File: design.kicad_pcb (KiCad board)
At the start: 2 copper layers, 136.2 x 88.1 mm, 170 parts, among them J1 TYPE-C-31-M-12, U1 TTP223, U10 ATtiny1616-M, U2 TTP223, U3 TTP223, U4 TTP223, U5 TTP223, U6 TTP223, U7 TTP223, U8 TTP223, U9 MAX77751CEFG_T

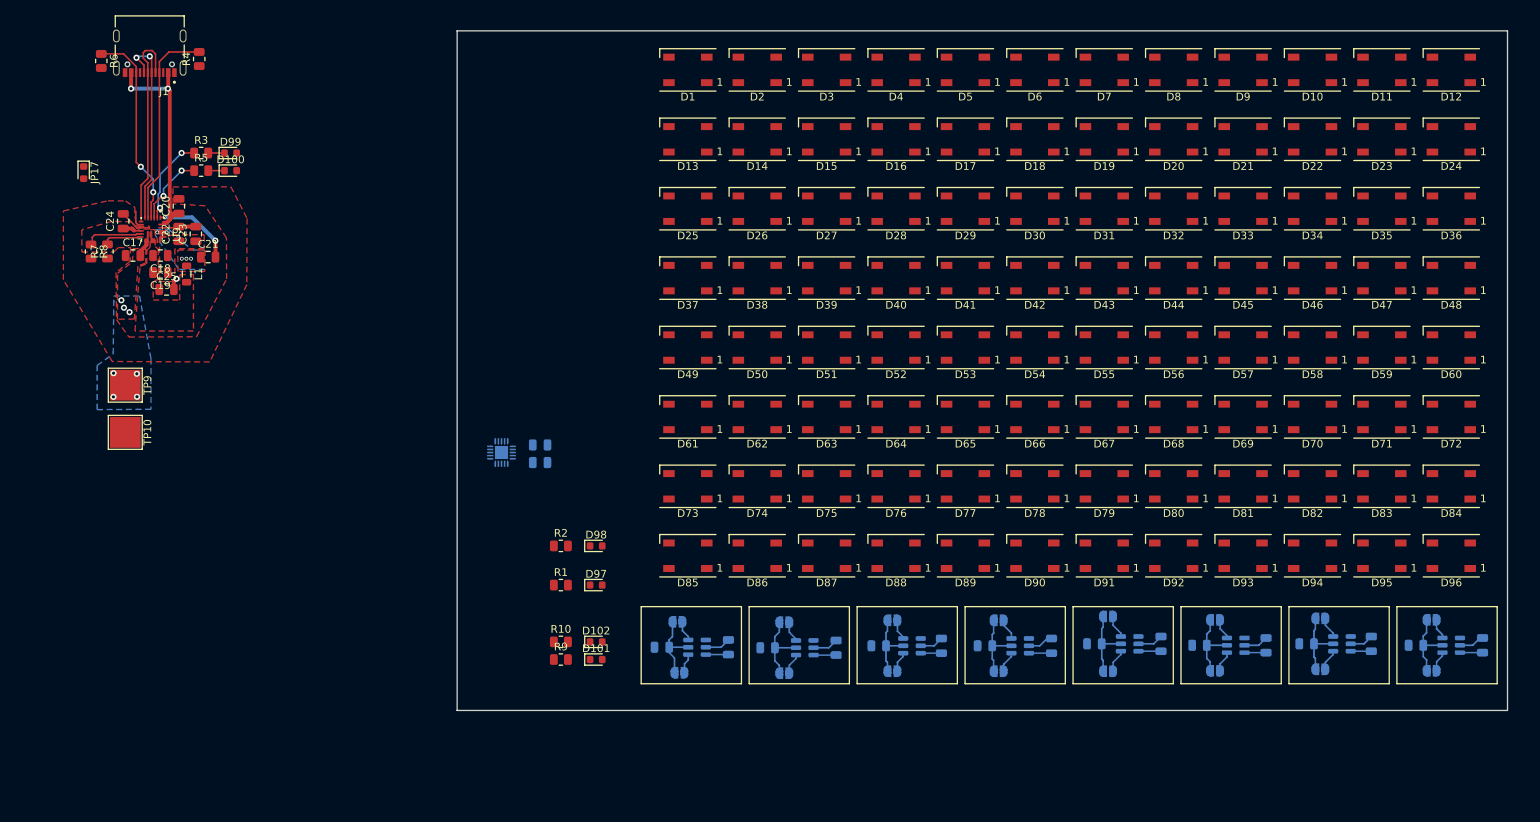
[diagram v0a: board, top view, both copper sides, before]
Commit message: some confusing LED double footprints
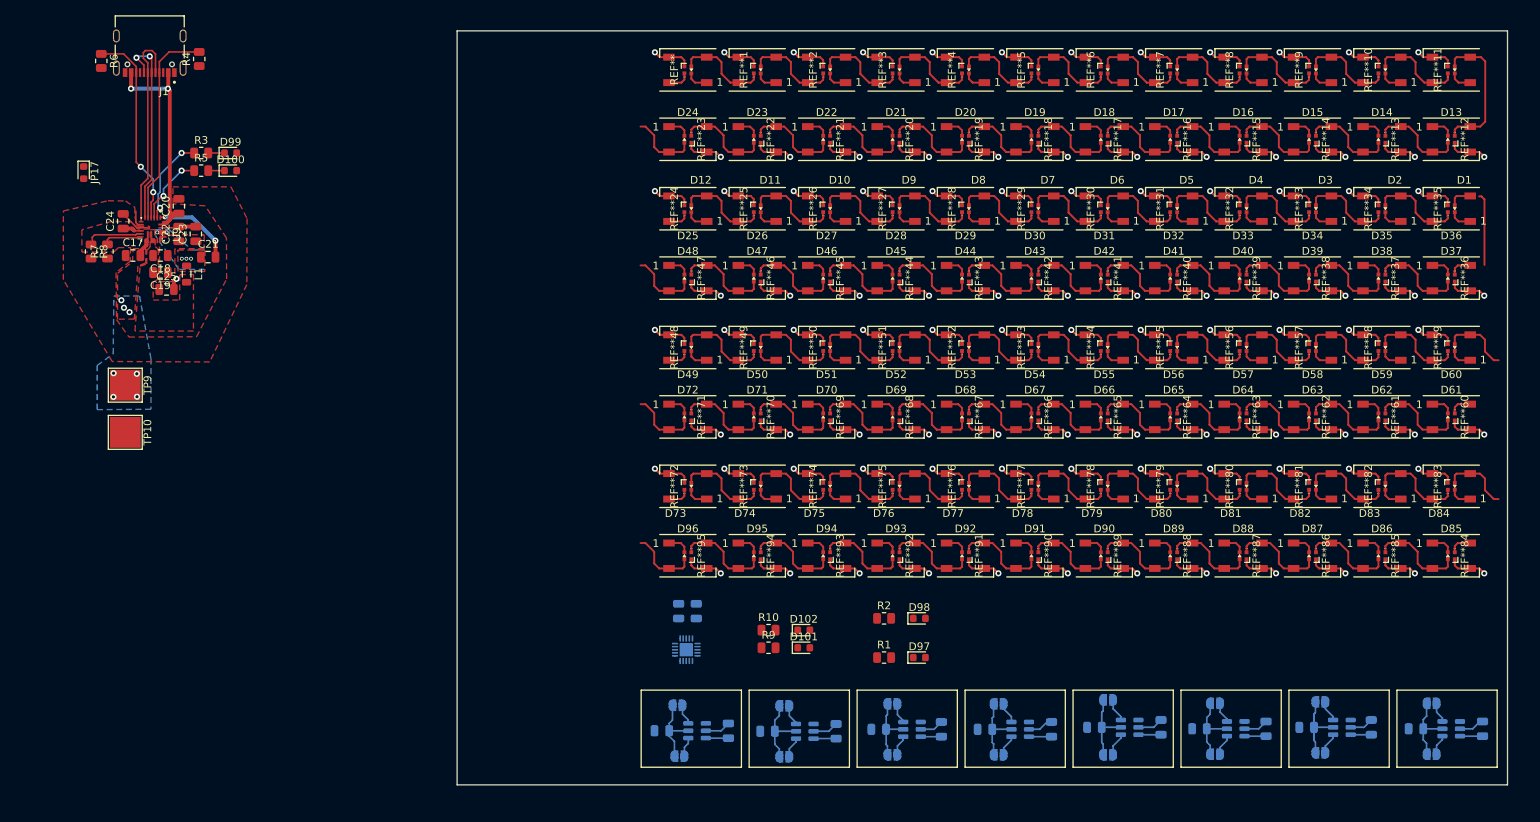
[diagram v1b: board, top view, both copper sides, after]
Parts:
- added REF**: LED_SK6805_EC15_1.5x1.5mm, LED_custom:LED_SK6805_EC15_1.5x1.5mm, F.Cu at (139.4, 57.4)
- added REF**1: LED_SK6805_EC15_1.5x1.5mm, LED_custom:LED_SK6805_EC15_1.5x1.5mm, F.Cu at (148.4, 57.4)
- added REF**10: LED_SK6805_EC15_1.5x1.5mm, LED_custom:LED_SK6805_EC15_1.5x1.5mm, F.Cu at (229.4, 57.4)
- added REF**11: LED_SK6805_EC15_1.5x1.5mm, LED_custom:LED_SK6805_EC15_1.5x1.5mm, F.Cu at (238.4, 57.4)
- added REF**12: LED_SK6805_EC15_1.5x1.5mm, LED_custom:LED_SK6805_EC15_1.5x1.5mm, F.Cu at (238.4, 66.4)
- added REF**13: LED_SK6805_EC15_1.5x1.5mm, LED_custom:LED_SK6805_EC15_1.5x1.5mm, F.Cu at (229.4, 66.4)
- added REF**14: LED_SK6805_EC15_1.5x1.5mm, LED_custom:LED_SK6805_EC15_1.5x1.5mm, F.Cu at (220.4, 66.4)
- added REF**15: LED_SK6805_EC15_1.5x1.5mm, LED_custom:LED_SK6805_EC15_1.5x1.5mm, F.Cu at (211.4, 66.4)
- added REF**16: LED_SK6805_EC15_1.5x1.5mm, LED_custom:LED_SK6805_EC15_1.5x1.5mm, F.Cu at (202.4, 66.4)
- added REF**17: LED_SK6805_EC15_1.5x1.5mm, LED_custom:LED_SK6805_EC15_1.5x1.5mm, F.Cu at (193.4, 66.4)
- added REF**18: LED_SK6805_EC15_1.5x1.5mm, LED_custom:LED_SK6805_EC15_1.5x1.5mm, F.Cu at (184.4, 66.4)
- added REF**19: LED_SK6805_EC15_1.5x1.5mm, LED_custom:LED_SK6805_EC15_1.5x1.5mm, F.Cu at (175.4, 66.4)
- added REF**2: LED_SK6805_EC15_1.5x1.5mm, LED_custom:LED_SK6805_EC15_1.5x1.5mm, F.Cu at (157.4, 57.4)
- added REF**20: LED_SK6805_EC15_1.5x1.5mm, LED_custom:LED_SK6805_EC15_1.5x1.5mm, F.Cu at (166.4, 66.4)
- added REF**21: LED_SK6805_EC15_1.5x1.5mm, LED_custom:LED_SK6805_EC15_1.5x1.5mm, F.Cu at (157.4, 66.4)
- added REF**22: LED_SK6805_EC15_1.5x1.5mm, LED_custom:LED_SK6805_EC15_1.5x1.5mm, F.Cu at (148.4, 66.4)
- added REF**23: LED_SK6805_EC15_1.5x1.5mm, LED_custom:LED_SK6805_EC15_1.5x1.5mm, F.Cu at (139.4, 66.4)
- added REF**24: LED_SK6805_EC15_1.5x1.5mm, LED_custom:LED_SK6805_EC15_1.5x1.5mm, F.Cu at (139.4, 75.4)
- added REF**25: LED_SK6805_EC15_1.5x1.5mm, LED_custom:LED_SK6805_EC15_1.5x1.5mm, F.Cu at (148.4, 75.4)
- added REF**26: LED_SK6805_EC15_1.5x1.5mm, LED_custom:LED_SK6805_EC15_1.5x1.5mm, F.Cu at (157.4, 75.4)
- added REF**27: LED_SK6805_EC15_1.5x1.5mm, LED_custom:LED_SK6805_EC15_1.5x1.5mm, F.Cu at (166.4, 75.4)
- added REF**28: LED_SK6805_EC15_1.5x1.5mm, LED_custom:LED_SK6805_EC15_1.5x1.5mm, F.Cu at (175.4, 75.4)
- added REF**29: LED_SK6805_EC15_1.5x1.5mm, LED_custom:LED_SK6805_EC15_1.5x1.5mm, F.Cu at (184.4, 75.4)
- added REF**3: LED_SK6805_EC15_1.5x1.5mm, LED_custom:LED_SK6805_EC15_1.5x1.5mm, F.Cu at (166.4, 57.4)
- added REF**30: LED_SK6805_EC15_1.5x1.5mm, LED_custom:LED_SK6805_EC15_1.5x1.5mm, F.Cu at (193.4, 75.4)
- added REF**31: LED_SK6805_EC15_1.5x1.5mm, LED_custom:LED_SK6805_EC15_1.5x1.5mm, F.Cu at (202.4, 75.4)
- added REF**32: LED_SK6805_EC15_1.5x1.5mm, LED_custom:LED_SK6805_EC15_1.5x1.5mm, F.Cu at (211.4, 75.4)
- added REF**33: LED_SK6805_EC15_1.5x1.5mm, LED_custom:LED_SK6805_EC15_1.5x1.5mm, F.Cu at (220.4, 75.4)
- added REF**34: LED_SK6805_EC15_1.5x1.5mm, LED_custom:LED_SK6805_EC15_1.5x1.5mm, F.Cu at (229.4, 75.4)
- added REF**35: LED_SK6805_EC15_1.5x1.5mm, LED_custom:LED_SK6805_EC15_1.5x1.5mm, F.Cu at (238.4, 75.4)
- added REF**36: LED_SK6805_EC15_1.5x1.5mm, LED_custom:LED_SK6805_EC15_1.5x1.5mm, F.Cu at (238.4, 84.4)
- added REF**37: LED_SK6805_EC15_1.5x1.5mm, LED_custom:LED_SK6805_EC15_1.5x1.5mm, F.Cu at (229.4, 84.4)
- added REF**38: LED_SK6805_EC15_1.5x1.5mm, LED_custom:LED_SK6805_EC15_1.5x1.5mm, F.Cu at (220.4, 84.4)
- added REF**39: LED_SK6805_EC15_1.5x1.5mm, LED_custom:LED_SK6805_EC15_1.5x1.5mm, F.Cu at (211.4, 84.4)
- added REF**4: LED_SK6805_EC15_1.5x1.5mm, LED_custom:LED_SK6805_EC15_1.5x1.5mm, F.Cu at (175.4, 57.4)
- added REF**40: LED_SK6805_EC15_1.5x1.5mm, LED_custom:LED_SK6805_EC15_1.5x1.5mm, F.Cu at (202.4, 84.4)
- added REF**41: LED_SK6805_EC15_1.5x1.5mm, LED_custom:LED_SK6805_EC15_1.5x1.5mm, F.Cu at (193.4, 84.4)
- added REF**42: LED_SK6805_EC15_1.5x1.5mm, LED_custom:LED_SK6805_EC15_1.5x1.5mm, F.Cu at (184.4, 84.4)
- added REF**43: LED_SK6805_EC15_1.5x1.5mm, LED_custom:LED_SK6805_EC15_1.5x1.5mm, F.Cu at (175.4, 84.4)
- added REF**44: LED_SK6805_EC15_1.5x1.5mm, LED_custom:LED_SK6805_EC15_1.5x1.5mm, F.Cu at (166.4, 84.4)
- added REF**45: LED_SK6805_EC15_1.5x1.5mm, LED_custom:LED_SK6805_EC15_1.5x1.5mm, F.Cu at (157.4, 84.4)
- added REF**46: LED_SK6805_EC15_1.5x1.5mm, LED_custom:LED_SK6805_EC15_1.5x1.5mm, F.Cu at (148.4, 84.4)
- added REF**47: LED_SK6805_EC15_1.5x1.5mm, LED_custom:LED_SK6805_EC15_1.5x1.5mm, F.Cu at (139.4, 84.4)
- added REF**48: LED_SK6805_EC15_1.5x1.5mm, LED_custom:LED_SK6805_EC15_1.5x1.5mm, F.Cu at (139.4, 93.4)
- added REF**49: LED_SK6805_EC15_1.5x1.5mm, LED_custom:LED_SK6805_EC15_1.5x1.5mm, F.Cu at (148.4, 93.4)
- added REF**5: LED_SK6805_EC15_1.5x1.5mm, LED_custom:LED_SK6805_EC15_1.5x1.5mm, F.Cu at (184.4, 57.4)
- added REF**50: LED_SK6805_EC15_1.5x1.5mm, LED_custom:LED_SK6805_EC15_1.5x1.5mm, F.Cu at (157.4, 93.4)
- added REF**51: LED_SK6805_EC15_1.5x1.5mm, LED_custom:LED_SK6805_EC15_1.5x1.5mm, F.Cu at (166.4, 93.4)
- added REF**52: LED_SK6805_EC15_1.5x1.5mm, LED_custom:LED_SK6805_EC15_1.5x1.5mm, F.Cu at (175.4, 93.4)
- added REF**53: LED_SK6805_EC15_1.5x1.5mm, LED_custom:LED_SK6805_EC15_1.5x1.5mm, F.Cu at (184.4, 93.4)
- added REF**54: LED_SK6805_EC15_1.5x1.5mm, LED_custom:LED_SK6805_EC15_1.5x1.5mm, F.Cu at (193.4, 93.4)
- added REF**55: LED_SK6805_EC15_1.5x1.5mm, LED_custom:LED_SK6805_EC15_1.5x1.5mm, F.Cu at (202.4, 93.4)
- added REF**56: LED_SK6805_EC15_1.5x1.5mm, LED_custom:LED_SK6805_EC15_1.5x1.5mm, F.Cu at (211.4, 93.4)
- added REF**57: LED_SK6805_EC15_1.5x1.5mm, LED_custom:LED_SK6805_EC15_1.5x1.5mm, F.Cu at (220.4, 93.4)
- added REF**58: LED_SK6805_EC15_1.5x1.5mm, LED_custom:LED_SK6805_EC15_1.5x1.5mm, F.Cu at (229.4, 93.4)
- added REF**59: LED_SK6805_EC15_1.5x1.5mm, LED_custom:LED_SK6805_EC15_1.5x1.5mm, F.Cu at (238.4, 93.4)
- added REF**6: LED_SK6805_EC15_1.5x1.5mm, LED_custom:LED_SK6805_EC15_1.5x1.5mm, F.Cu at (193.4, 57.4)
- added REF**60: LED_SK6805_EC15_1.5x1.5mm, LED_custom:LED_SK6805_EC15_1.5x1.5mm, F.Cu at (238.4, 102.4)
- added REF**61: LED_SK6805_EC15_1.5x1.5mm, LED_custom:LED_SK6805_EC15_1.5x1.5mm, F.Cu at (229.4, 102.4)
- added REF**62: LED_SK6805_EC15_1.5x1.5mm, LED_custom:LED_SK6805_EC15_1.5x1.5mm, F.Cu at (220.4, 102.4)
- added REF**63: LED_SK6805_EC15_1.5x1.5mm, LED_custom:LED_SK6805_EC15_1.5x1.5mm, F.Cu at (211.4, 102.4)
- added REF**64: LED_SK6805_EC15_1.5x1.5mm, LED_custom:LED_SK6805_EC15_1.5x1.5mm, F.Cu at (202.4, 102.4)
- added REF**65: LED_SK6805_EC15_1.5x1.5mm, LED_custom:LED_SK6805_EC15_1.5x1.5mm, F.Cu at (193.4, 102.4)
- added REF**66: LED_SK6805_EC15_1.5x1.5mm, LED_custom:LED_SK6805_EC15_1.5x1.5mm, F.Cu at (184.4, 102.4)
- added REF**67: LED_SK6805_EC15_1.5x1.5mm, LED_custom:LED_SK6805_EC15_1.5x1.5mm, F.Cu at (175.4, 102.4)
- added REF**68: LED_SK6805_EC15_1.5x1.5mm, LED_custom:LED_SK6805_EC15_1.5x1.5mm, F.Cu at (166.4, 102.4)
- added REF**69: LED_SK6805_EC15_1.5x1.5mm, LED_custom:LED_SK6805_EC15_1.5x1.5mm, F.Cu at (157.4, 102.4)
- added REF**7: LED_SK6805_EC15_1.5x1.5mm, LED_custom:LED_SK6805_EC15_1.5x1.5mm, F.Cu at (202.4, 57.4)
- added REF**70: LED_SK6805_EC15_1.5x1.5mm, LED_custom:LED_SK6805_EC15_1.5x1.5mm, F.Cu at (148.4, 102.4)
- added REF**71: LED_SK6805_EC15_1.5x1.5mm, LED_custom:LED_SK6805_EC15_1.5x1.5mm, F.Cu at (139.4, 102.4)
- added REF**72: LED_SK6805_EC15_1.5x1.5mm, LED_custom:LED_SK6805_EC15_1.5x1.5mm, F.Cu at (139.4, 111.4)
- added REF**73: LED_SK6805_EC15_1.5x1.5mm, LED_custom:LED_SK6805_EC15_1.5x1.5mm, F.Cu at (148.4, 111.4)
- added REF**74: LED_SK6805_EC15_1.5x1.5mm, LED_custom:LED_SK6805_EC15_1.5x1.5mm, F.Cu at (157.4, 111.4)
- added REF**75: LED_SK6805_EC15_1.5x1.5mm, LED_custom:LED_SK6805_EC15_1.5x1.5mm, F.Cu at (166.4, 111.4)
- added REF**76: LED_SK6805_EC15_1.5x1.5mm, LED_custom:LED_SK6805_EC15_1.5x1.5mm, F.Cu at (175.4, 111.4)
- added REF**77: LED_SK6805_EC15_1.5x1.5mm, LED_custom:LED_SK6805_EC15_1.5x1.5mm, F.Cu at (184.4, 111.4)
- added REF**78: LED_SK6805_EC15_1.5x1.5mm, LED_custom:LED_SK6805_EC15_1.5x1.5mm, F.Cu at (193.4, 111.4)
- added REF**79: LED_SK6805_EC15_1.5x1.5mm, LED_custom:LED_SK6805_EC15_1.5x1.5mm, F.Cu at (202.4, 111.4)
- added REF**8: LED_SK6805_EC15_1.5x1.5mm, LED_custom:LED_SK6805_EC15_1.5x1.5mm, F.Cu at (211.4, 57.4)
- added REF**80: LED_SK6805_EC15_1.5x1.5mm, LED_custom:LED_SK6805_EC15_1.5x1.5mm, F.Cu at (211.4, 111.4)
- added REF**81: LED_SK6805_EC15_1.5x1.5mm, LED_custom:LED_SK6805_EC15_1.5x1.5mm, F.Cu at (220.4, 111.4)
- added REF**82: LED_SK6805_EC15_1.5x1.5mm, LED_custom:LED_SK6805_EC15_1.5x1.5mm, F.Cu at (229.4, 111.4)
- added REF**83: LED_SK6805_EC15_1.5x1.5mm, LED_custom:LED_SK6805_EC15_1.5x1.5mm, F.Cu at (238.4, 111.4)
- added REF**84: LED_SK6805_EC15_1.5x1.5mm, LED_custom:LED_SK6805_EC15_1.5x1.5mm, F.Cu at (238.4, 120.4)
- added REF**85: LED_SK6805_EC15_1.5x1.5mm, LED_custom:LED_SK6805_EC15_1.5x1.5mm, F.Cu at (229.4, 120.4)
- added REF**86: LED_SK6805_EC15_1.5x1.5mm, LED_custom:LED_SK6805_EC15_1.5x1.5mm, F.Cu at (220.4, 120.4)
- added REF**87: LED_SK6805_EC15_1.5x1.5mm, LED_custom:LED_SK6805_EC15_1.5x1.5mm, F.Cu at (211.4, 120.4)
- added REF**88: LED_SK6805_EC15_1.5x1.5mm, LED_custom:LED_SK6805_EC15_1.5x1.5mm, F.Cu at (202.4, 120.4)
- added REF**89: LED_SK6805_EC15_1.5x1.5mm, LED_custom:LED_SK6805_EC15_1.5x1.5mm, F.Cu at (193.4, 120.4)
- added REF**9: LED_SK6805_EC15_1.5x1.5mm, LED_custom:LED_SK6805_EC15_1.5x1.5mm, F.Cu at (220.4, 57.4)
- added REF**90: LED_SK6805_EC15_1.5x1.5mm, LED_custom:LED_SK6805_EC15_1.5x1.5mm, F.Cu at (184.4, 120.4)
- added REF**91: LED_SK6805_EC15_1.5x1.5mm, LED_custom:LED_SK6805_EC15_1.5x1.5mm, F.Cu at (175.4, 120.4)
- added REF**92: LED_SK6805_EC15_1.5x1.5mm, LED_custom:LED_SK6805_EC15_1.5x1.5mm, F.Cu at (166.4, 120.4)
- added REF**93: LED_SK6805_EC15_1.5x1.5mm, LED_custom:LED_SK6805_EC15_1.5x1.5mm, F.Cu at (157.4, 120.4)
- added REF**94: LED_SK6805_EC15_1.5x1.5mm, LED_custom:LED_SK6805_EC15_1.5x1.5mm, F.Cu at (148.4, 120.4)
- added REF**95: LED_SK6805_EC15_1.5x1.5mm, LED_custom:LED_SK6805_EC15_1.5x1.5mm, F.Cu at (139.4, 120.4)
- moved D13 99.0 mm to (238.4, 66.4), turned to 0 degrees
- moved D24 99.0 mm to (139.4, 66.4), turned to 0 degrees
- moved D37 99.0 mm to (238.4, 84.4), turned to 0 degrees
- moved D48 99.0 mm to (139.4, 84.4), turned to 0 degrees
- moved D61 99.0 mm to (238.4, 102.4), turned to 0 degrees
- moved D72 99.0 mm to (139.4, 102.4), turned to 0 degrees
- moved D85 99.0 mm to (238.4, 120.4), turned to 0 degrees
- moved D96 99.0 mm to (139.4, 120.4), turned to 0 degrees
- moved D14 81.0 mm to (229.4, 66.4), turned to 0 degrees
- moved D23 81.0 mm to (148.4, 66.4), turned to 0 degrees
- moved D38 81.0 mm to (229.4, 84.4), turned to 0 degrees
- moved D47 81.0 mm to (148.4, 84.4), turned to 0 degrees
- moved D62 81.0 mm to (229.4, 102.4), turned to 0 degrees
- moved D71 81.0 mm to (148.4, 102.4), turned to 0 degrees
- moved D86 81.0 mm to (229.4, 120.4), turned to 0 degrees
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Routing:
- net Net-(D1-Pad2): track 0.00 -> 852.4 mm
- net GND: track 30.5 -> 515.5 mm, vias 1 -> 97
- net in: track 0.00 -> 285.4 mm
- net +5V: track 0.00 -> 280.2 mm
- net 1out: track 0.00 -> 11.4 mm
- net (no net): track 0.00 -> 9.07 mm
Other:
- board size 136.2 x 88.1 mm -> 136.2 x 97.8 mm

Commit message: new layout
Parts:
- removed REF**, REF**1, REF**10, REF**11, REF**12, REF**13, REF**14, REF**15, REF**16, REF**17, REF**18, REF**19, REF**2, REF**20, REF**21, REF**22, REF**23, REF**24, REF**25, REF**26, REF**27, REF**28, REF**29, REF**3, REF**30, REF**31, REF**32, REF**33, REF**34, REF**35, REF**36, REF**37, REF**38, REF**39, REF**4, REF**40, REF**41, REF**42, REF**43, REF**44, REF**45, REF**46, REF**47, REF**48, REF**49, REF**5, REF**50, REF**51, REF**52, REF**53, REF**54, REF**55, REF**56, REF**57, REF**58, REF**59, REF**6, REF**60, REF**61, REF**62, REF**63, REF**64, REF**65, REF**66, REF**67, REF**68, REF**69, REF**7, REF**70, REF**71, REF**72, REF**73, REF**74, REF**75, REF**76, REF**77, REF**78, REF**79, REF**8, REF**80, REF**81, REF**82, REF**83, REF**84, REF**85, REF**86, REF**87, REF**88, REF**89, REF**9, REF**90, REF**91, REF**92, REF**93, REF**94, REF**95: LED_SK6805_EC15_1.5x1.5mm, LED_custom:LED_SK6805_EC15_1.5x1.5mm
- C26, C27: moved to F.Cu
- moved D12 118.4 mm to (138.3, 120.6), turned to 0 degrees
- moved D85 118.2 mm to (138.3, 57.6), turned to 180 degrees
- moved D1 116.5 mm to (237.3, 120.6), turned to 0 degrees
- moved D96 116.3 mm to (237.3, 57.6), turned to 180 degrees
- moved D13 109.8 mm to (138.3, 111.6), turned to 180 degrees
- moved D84 109.7 mm to (138.3, 66.6), turned to 0 degrees
- moved D24 107.8 mm to (237.3, 111.6), turned to 180 degrees
- moved D73 107.7 mm to (237.3, 66.6), turned to 0 degrees
- moved D36 103.7 mm to (138.3, 102.6), turned to 0 degrees
- moved D61 103.6 mm to (138.3, 75.6), turned to 180 degrees
- moved D11 103.6 mm to (147.3, 120.6), turned to 0 degrees
- moved D86 103.4 mm to (147.3, 57.6), turned to 180 degrees
- moved D2 101.9 mm to (228.3, 120.6), turned to 0 degrees
- moved D95 101.6 mm to (228.3, 57.6), turned to 180 degrees
- moved D25 101.6 mm to (237.3, 102.6), turned to 0 degrees
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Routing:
- net Net-(D1-Pad2): track 852.4 -> 6.46 mm
- net GND: track 515.5 -> 30.5 mm, vias 97 -> 1
- net in: track 285.4 -> 0.00 mm
- net +5V: track 280.2 -> 240.0 mm
- net 6out: track 0.00 -> 13.4 mm
- net 4out: track 0.00 -> 12.4 mm
- net 3out: track 0.30 -> 12.7 mm, vias 0 -> 2
- net 5out: track 0.00 -> 12.3 mm, vias 0 -> 2
- net 7out: track 0.00 -> 12.3 mm, vias 0 -> 2
- net 2out: track 0.00 -> 12.2 mm
- net (no net): track 9.07 -> 0.00 mm
- net Net-(D83-Pad2): track 0.00 -> 6.46 mm
- net Net-(D82-Pad2): track 0.00 -> 6.46 mm
- net Net-(D81-Pad2): track 0.00 -> 6.46 mm
- net Net-(D80-Pad2): track 0.00 -> 6.46 mm
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
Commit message: updates
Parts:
- added J301: TYPE-C-31-M-12, Snapeda:TYPE-C-31-M-12_HRO_TYPE-C-31-M-12, B.Cu at (128.5, 130.5)
- added R301: 5.1k, Resistor_SMD:R_0805_2012Metric, B.Cu at (131.6, 136.6)
- added R302: 5.1k, Resistor_SMD:R_0805_2012Metric, B.Cu at (131.4, 124.4)
- C26, C27: moved to B.Cu
- moved D98 128.6 mm to (58.2, 64.0)
- moved R2 128.6 mm to (53.6, 64.0)
- moved C26 64.8 mm to (186.6, 125.6), turned to 180 degrees
- moved C27 60.1 mm to (186.6, 127.8), turned to 180 degrees
- moved D101 45.4 mm to (199.8, 129.7)
- moved R9 45.4 mm to (195.2, 129.7)
- moved D102 45.4 mm to (199.8, 131.8)
- moved R10 45.4 mm to (195.2, 131.8)
- moved D97 28.2 mm to (141.4, 130.6), turned to 180 degrees
- moved R1 19.1 mm to (146.0, 130.6), turned to 180 degrees
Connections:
- R10 pad 1: Net-(R10-Pad1) -> Net-(U10-Pad7)
- R9 pad 1: Net-(R9-Pad1) -> Net-(U10-Pad6)
- U10 pad 1: in -> unconnected-(U10-Pad1)
- U10 pad 10: touch_point_7 -> touch_state_6
- U10 pad 11: touch_point_6 -> touch_state_5
- U10 pad 12: touch_point_5 -> unconnected-(U10-Pad12)
- U10 pad 13: touch_point_4 -> unconnected-(U10-Pad13)
- U10 pad 14: touch_point_3 -> unconnected-(U10-Pad14)
- U10 pad 15: Net-(R9-Pad1) -> touch_state_4
- U10 pad 16: Net-(R10-Pad1) -> touch_state_3
- U10 pad 17: unconnected-(U10-Pad17) -> touch_state_2
- U10 pad 18: unconnected-(U10-Pad18) -> touch_state_1
- U10 pad 5: unconnected-(U10-Pad5) -> in
- U10 pad 6: unconnected-(U10-Pad6) -> Net-(U10-Pad6)
- U10 pad 7: touch_point_1 -> Net-(U10-Pad7)
- U10 pad 8: touch_point_2 -> touch_state_8
- U10 pad 9: touch_point_8 -> touch_state_7
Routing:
- net touch_state_8: track 0.00 -> 59.4 mm
- net in: track 0.00 -> 58.5 mm, vias 0 -> 1
- net touch_state_1: track 0.00 -> 48.9 mm
- net touch_state_7: track 0.00 -> 44.8 mm
- net +5V: track 240.0 -> 282.0 mm, vias 0 -> 2
- net touch_state_2: track 0.00 -> 37.4 mm
- net touch_state_6: track 0.00 -> 30.3 mm
- net touch_state_3: track 0.00 -> 23.4 mm
- net touch_state_5: track 0.00 -> 17.5 mm
- net touch_state_4: track 0.00 -> 10.2 mm
- net Net-(U10-Pad7): track 0.00 -> 7.02 mm, vias 0 -> 1
- net Net-(J301-PadA5): track 0.00 -> 6.95 mm
- net Net-(U10-Pad6): track 0.00 -> 6.82 mm, vias 0 -> 1
- net Net-(J301-PadB5): track 0.00 -> 6.77 mm
- net GND: track 30.5 -> 34.8 mm
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- added copper zone on F.Cu, net touch_point_1
- added copper zone on F.Cu, net touch_point_2
- added copper zone on F.Cu, net touch_point_3
- added copper zone on F.Cu, net touch_point_4
- added copper zone on F.Cu, net touch_point_5
- added copper zone on F.Cu, net touch_point_6
- added copper zone on F.Cu, net touch_point_7
- added copper zone on F.Cu, net touch_point_8
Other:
- board size 136.2 x 97.8 mm -> 119.3 x 97.8 mm
- board text added: "+ ->"
- board text added: "->"
- board text added: "Clear"
- board text added: "Color"
- board text added: "DIR"
- board text added: "DIR ->"
- board text added: "NEXT"

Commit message: Update design.kicad_pcb
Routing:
- net GND: vias 1 -> 8
- added copper zone on B.Cu, net GND
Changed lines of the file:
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@@
   (segment (start 73.08 84.492) (end 72.75 84.822) (width 0.5) (layer "F.Cu") (net 2))
   (segment (start 72.75 84.822) (end 72.75 85.872) (width 0.5) (layer "F.Cu") (net 2))
+  (via (at 135.8 124.7) (size 0.8) (drill 0.4) (layers "F.Cu" "B.Cu") (free) (net 2))
+  (via (at 138.3 135.8) (size 0.8) (drill 0.4) (layers "F.Cu" "B.Cu") (free) (net 2))
+  (via (at 205.2 129.4) (size 0.8) (drill 0.4) (layers "F.Cu" "B.Cu") (free) (net 2))
+  (via (at 128.6 132.4) (size 0.8) (drill 0.4) (layers "F.Cu" "B.Cu") (free) (net 2))
+  (via (at 128.6 129) (size 0.8) (drill 0.4) (layers "F.Cu" "B.Cu") (free) (net 2))
+  (via (at 205.2 132) (size 0.8) (drill 0.4) (layers "F.Cu" "B.Cu") (free) (net 2))
   (via (at 73.08 84.492) (size 0.8) (drill 0.4) (layers "F.Cu" "B.Cu") (net 2))
+  (via (at 150.7 130.8) (size 0.8) (drill 0.4) (layers "F.Cu" "B.Cu") (free) (net 2))
   (segment (start 143.7085 143.096) (end 144.6585 142.146) (width 0.21) (layer "B.Cu") (net 2))
   (segment (start 185.0335 142.908) (end 185.9835 141.958) (width 0.21) (layer "B.Cu") (net 2))
@@
   (segment (start 130.475 124.4) (end 130.475 128.175) (width 0.21) (layer "B.Cu") (net 171))
   (zone (net 8) (net_name "touch_point_8") (layer "F.Cu") (hatch edge 0.508)
+    (priority 1)
     (connect_pads (clearance 0.3))
     (min_thickness 0.254) (filled_areas_thickness no)
@@
   )
   (zone (net 1) (net_name "touch_point_3") (layer "F.Cu") (hatch edge 0.508)
+    (priority 1)
     (connect_pads (clearance 0.3))
     (min_thickness 0.254) (filled_areas_thickness no)
@@
   )
   (zone (net 11) (net_name "+5V") (layer "F.Cu") (hatch edge 0.508)
+    (priority 1)
     (connect_pads (clearance 0.3))
     (min_thickness 0.254) (filled_areas_thickness no)
@@
   )
   (zone (net 11) (net_name "+5V") (layer "F.Cu") (hatch edge 0.508)
+    (priority 1)
     (connect_pads (clearance 0.3))
     (min_thickness 0.254) (filled_areas_thickness no)
@@
   )
   (zone (net 10) (net_name "touch_point_6") (layer "F.Cu") (hatch edge 0.508)
+    (priority 1)
     (connect_pads (clearance 0.3))
     (min_thickness 0.254) (filled_areas_thickness no)
@@
   )
   (zone (net 7) (net_name "touch_point_7") (layer "F.Cu") (hatch edge 0.508)
+    (priority 1)
     (connect_pads (clearance 0.3))
     (min_thickness 0.254) (filled_areas_thickness no)
@@
   )
   (zone (net 11) (net_name "+5V") (layer "F.Cu") (hatch edge 0.508)
+    (priority 1)
     (connect_pads (clearance 0.3))
     (min_thickness 0.254) (filled_areas_thickness no)
@@
   )
   (zone (net 9) (net_name "touch_point_5") (layer "F.Cu") (hatch edge 0.508)
+    (priority 1)
     (connect_pads (clearance 0.3))
     (min_thickness 0.254) (filled_areas_thickness no)
@@
   )
   (zone (net 4) (net_name "touch_point_1") (layer "F.Cu") (hatch edge 0.508)
+    (priority 1)
     (connect_pads (clearance 0.3))
     (min_thickness 0.254) (filled_areas_thickness no)
@@
   )
   (zone (net 11) (net_name "+5V") (layer "F.Cu") (hatch edge 0.508)
+    (priority 1)
     (connect_pads (clearance 0.3))
     (min_thickness 0.254) (filled_areas_thickness no)
@@
     )
   )
+  (zone (net 2) (net_name "GND") (layers F&B.Cu) (hatch edge 0.508)
+    (connect_pads (clearance 0.3))
+    (min_thickness 0.254) (filled_areas_thickness no)
+    (fill yes (thermal_gap 0.508) (thermal_bridge_width 0.508))
+    (polygon
+      (pts
+        (xy 247.6 152.3)
+        (xy 124 152.9)
+        (xy 124.1 50.9)
+        (xy 247.9 50.8)
+      )
+    )
+  )
   (zone (net 5) (net_name "touch_point_2") (layer "F.Cu") (hatch edge 0.508)
+    (priority 1)
     (connect_pads (clearance 0.3))
     (min_thickness 0.254) (filled_areas_thickness no)
@@
   )
   (zone (net 3) (net_name "touch_point_4") (layer "F.Cu") (hatch edge 0.508)
+    (priority 1)
     (connect_pads (clearance 0.3))
     (min_thickness 0.254) (filled_areas_thickness no)
@@
   )
   (zone (net 11) (net_name "+5V") (layer "F.Cu") (hatch edge 0.508)
-    (connect_pads (clearance 0.3))
-    (min_thickness 0.254) (filled_areas_thickness no)
+    (priority 1)
+    (connect_pads (clearance 0.3))
+    (min_thickness 0.254) (filled_areas_thickness no)

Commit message: upadte
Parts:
- removed C17, C18, C19, C22: 10uF, Capacitor_SMD:C_0805_2012Metric
- removed C20, C24, C25: 2.2uF, Capacitor_SMD:C_0805_2012Metric
- removed C21: 0.1uF, Capacitor_SMD:C_0805_2012Metric
- removed C23: 22uF, Capacitor_SMD:C_0805_2012Metric
- removed D100: STAT, LED_SMD:LED_0603_1608Metric
- removed D98: VBUS, LED_SMD:LED_0603_1608Metric
- removed D99: INOKB, LED_SMD:LED_0603_1608Metric
- removed J1: TYPE-C-31-M-12, Snapeda:TYPE-C-31-M-12_HRO_TYPE-C-31-M-12
- removed JP17: ENBST, LED_SMD:LED_0603_1608Metric
- removed L1: 0.47uH, Inductor_SMD:L_0805_2012Metric
- removed R2, R3, R5: 1k, Resistor_SMD:R_0805_2012Metric
- removed R4, R6: 5.1k, Resistor_SMD:R_0805_2012Metric
- removed R7: 2.4k, Resistor_SMD:R_0805_2012Metric
- removed R8: 13.3k, Resistor_SMD:R_0805_2012Metric
- removed TP10: BAT-, TestPoint:TestPoint_Pad_4.0x4.0mm
- removed TP9: BAT+, TestPoint:TestPoint_Pad_4.0x4.0mm
- removed U9: MAX77751CEFG_T, Snapeda:IC_MAX77751CEFG_T
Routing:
- net VBUS: track 30.3 -> 0.00 mm, vias 2 -> 0
- net D-: track 26.8 -> 0.00 mm
- net CC1: track 26.5 -> 0.00 mm
- net CC2: track 25.8 -> 0.00 mm, vias 2 -> 0
- net D+: track 25.5 -> 0.00 mm, vias 2 -> 0
- net +5V: track 282.0 -> 297.4 mm
- net Net-(R3-Pad1): track 11.5 -> 0.00 mm, vias 2 -> 0
- net BST: track 10.5 -> 0.00 mm, vias 2 -> 0
- net Net-(R5-Pad1): track 9.32 -> 0.00 mm, vias 2 -> 0
- net Net-(R8-Pad1): track 7.52 -> 0.00 mm
- net Net-(R7-Pad2): track 5.12 -> 0.00 mm
- net GND: track 34.8 -> 30.2 mm
- net BYP: track 4.16 -> 0.00 mm
- net Net-(JP17-Pad1): track 2.27 -> 0.00 mm
- net BAT: track 2.23 -> 0.00 mm, vias 7 -> 0
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- removed copper zone on B.Cu, net BAT
- removed copper zone on F.Cu, net BAT
- removed copper zone on B.Cu, net LX
- removed copper zone on F.Cu, net LX

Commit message: update
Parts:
- added TP301: UPDI, TestPoint:TestPoint_Pad_3.0x3.0mm, B.Cu at (176.1, 127.2)
- added TP302: +5V, TestPoint:TestPoint_Pad_3.0x3.0mm, B.Cu at (166.0, 127.2)
- added TP303: GND, TestPoint:TestPoint_Pad_3.0x3.0mm, B.Cu at (171.1, 127.2)
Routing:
- net +5V: track 297.4 -> 308.4 mm, vias 2 -> 3
- net UPDI: track 0.00 -> 10.2 mm
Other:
- board text added: "Brightness"
- board text removed: "Color"
